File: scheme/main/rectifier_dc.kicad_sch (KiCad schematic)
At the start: 30 parts, among them K1 G2RL-1-E, Q2 BC847

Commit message: added L fuse & more
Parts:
- D15: footprint (none) -> LED_SMD:LED_0805_2012Metric
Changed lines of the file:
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@@
 			)
 		)
-		(property "Footprint" ""
+		(property "Footprint" "LED_SMD:LED_0805_2012Metric"
 			(at 250.19 74.93 0)
 			(effects

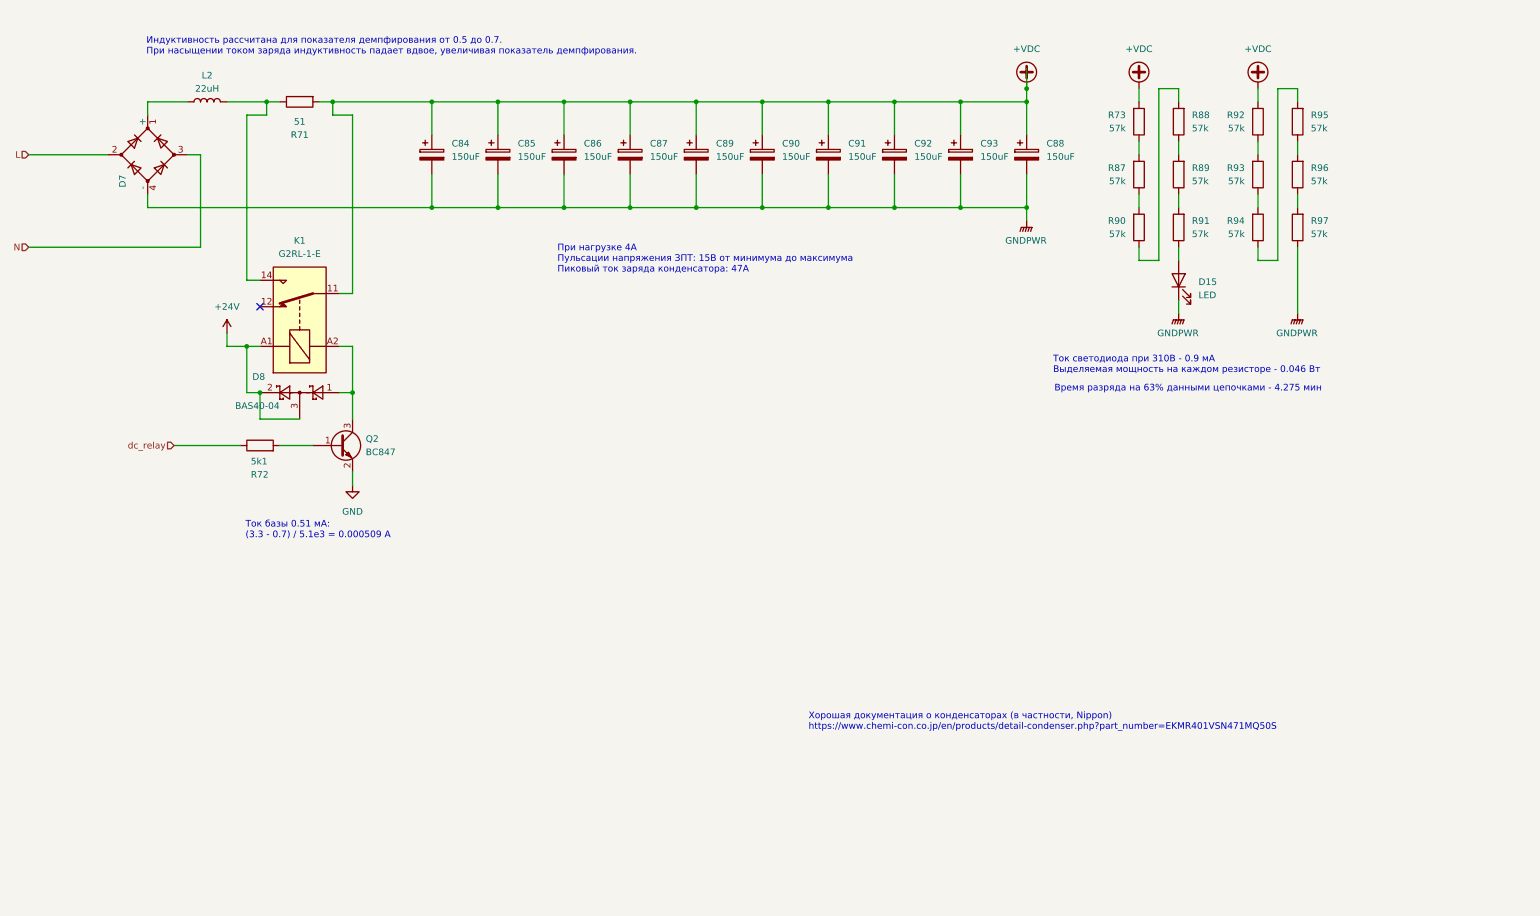
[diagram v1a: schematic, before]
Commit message: added 24V & GND to DO terminal & more
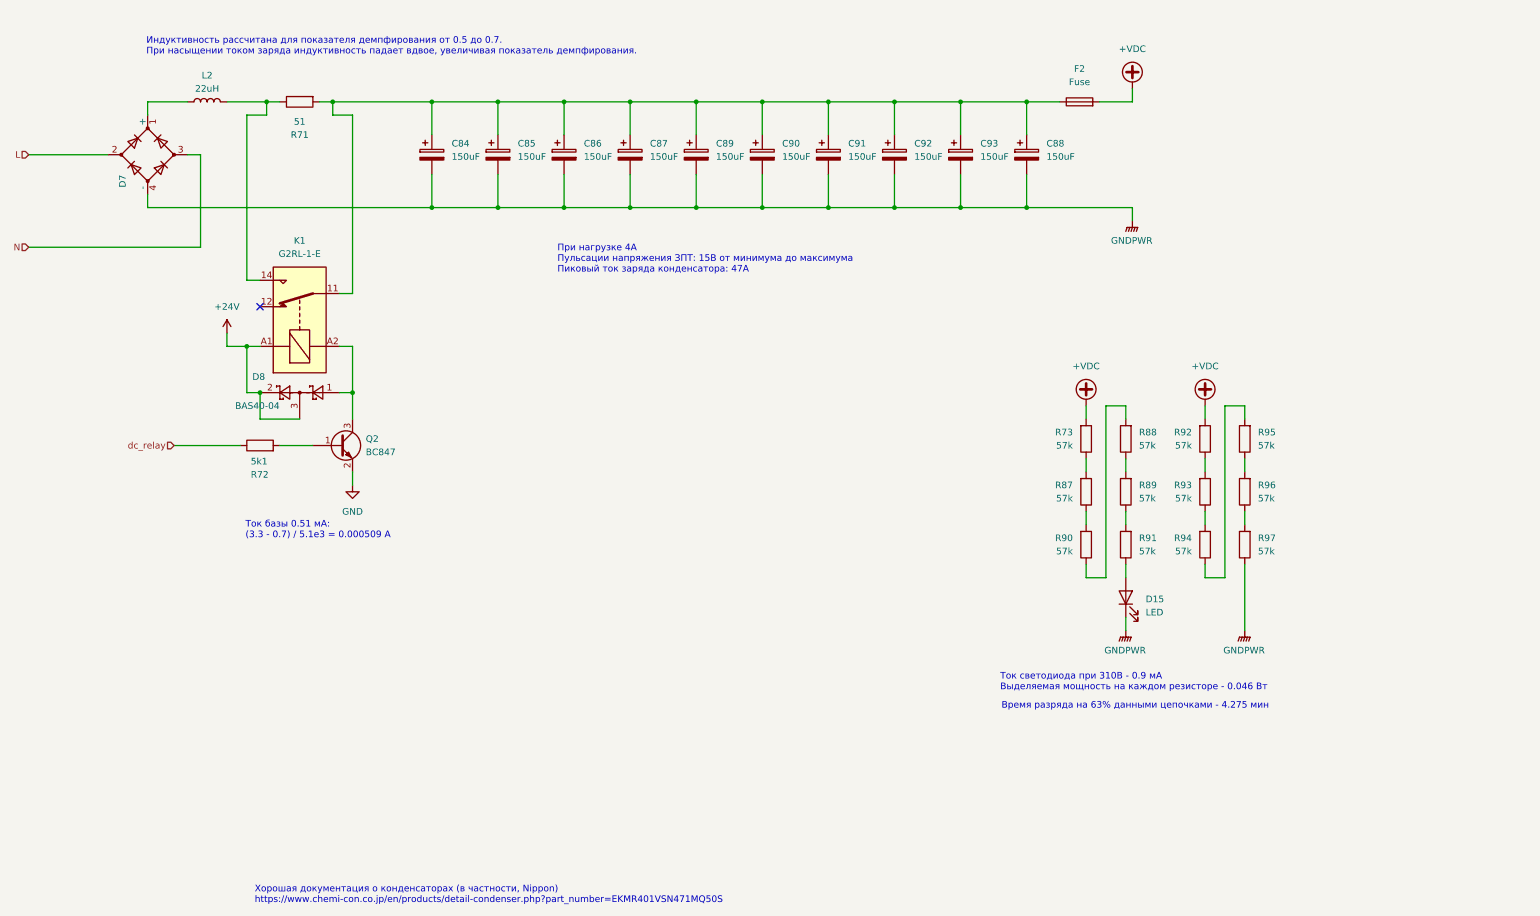
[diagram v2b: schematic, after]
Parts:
- added F2: Fuse, symbol Device:Fuse
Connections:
- net +VDC: now also F2.2; no longer C84.1, C85.1, C86.1, C87.1, C88.1, C89.1, C90.1, C91.1, C92.1, C93.1, K1.11, R71.2
- new net: C84.1, C85.1, C86.1, C87.1, C88.1, C89.1, C90.1, C91.1, C92.1, C93.1, F2.1, K1.11, R71.2
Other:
- moved on the sheet: D15, R73, R87, R88, R89, R90, R91, R92, R93, R94, R95, R96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

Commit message: sheets titles
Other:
- title: (none) -> Выпрямитель и звено постоянного тока
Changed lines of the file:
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@@
 	(generator_version "8.0")
 	(paper "A4")
+	(title_block
+		(title "Выпрямитель и звено постоянного тока")
+	)
 	(junction
 		(at 106.68 60.96)

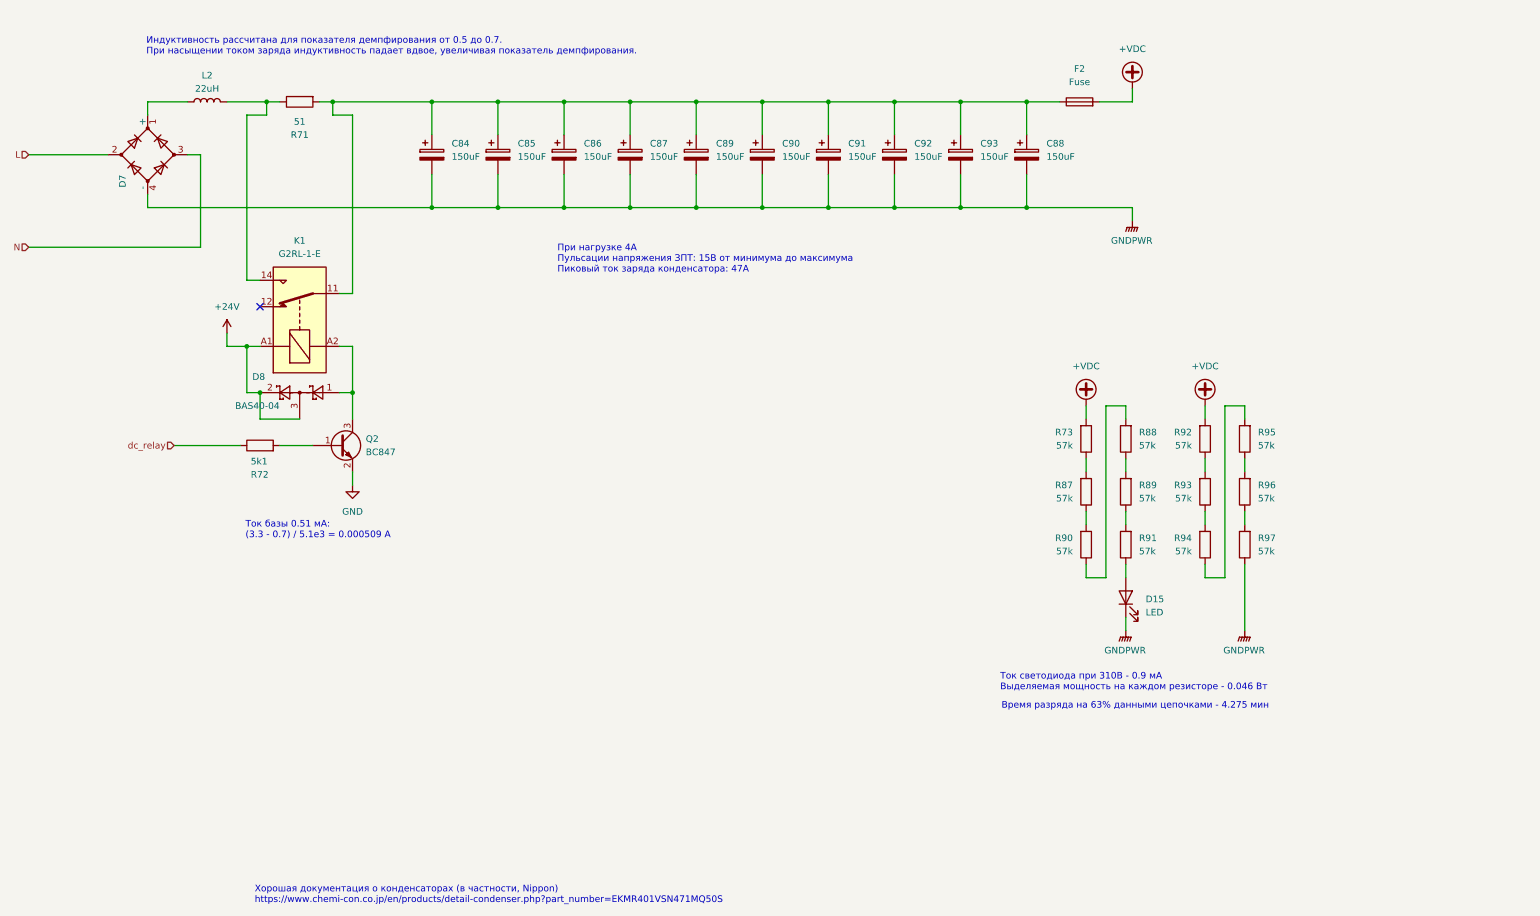
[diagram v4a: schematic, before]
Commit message: added fuses & inductanses
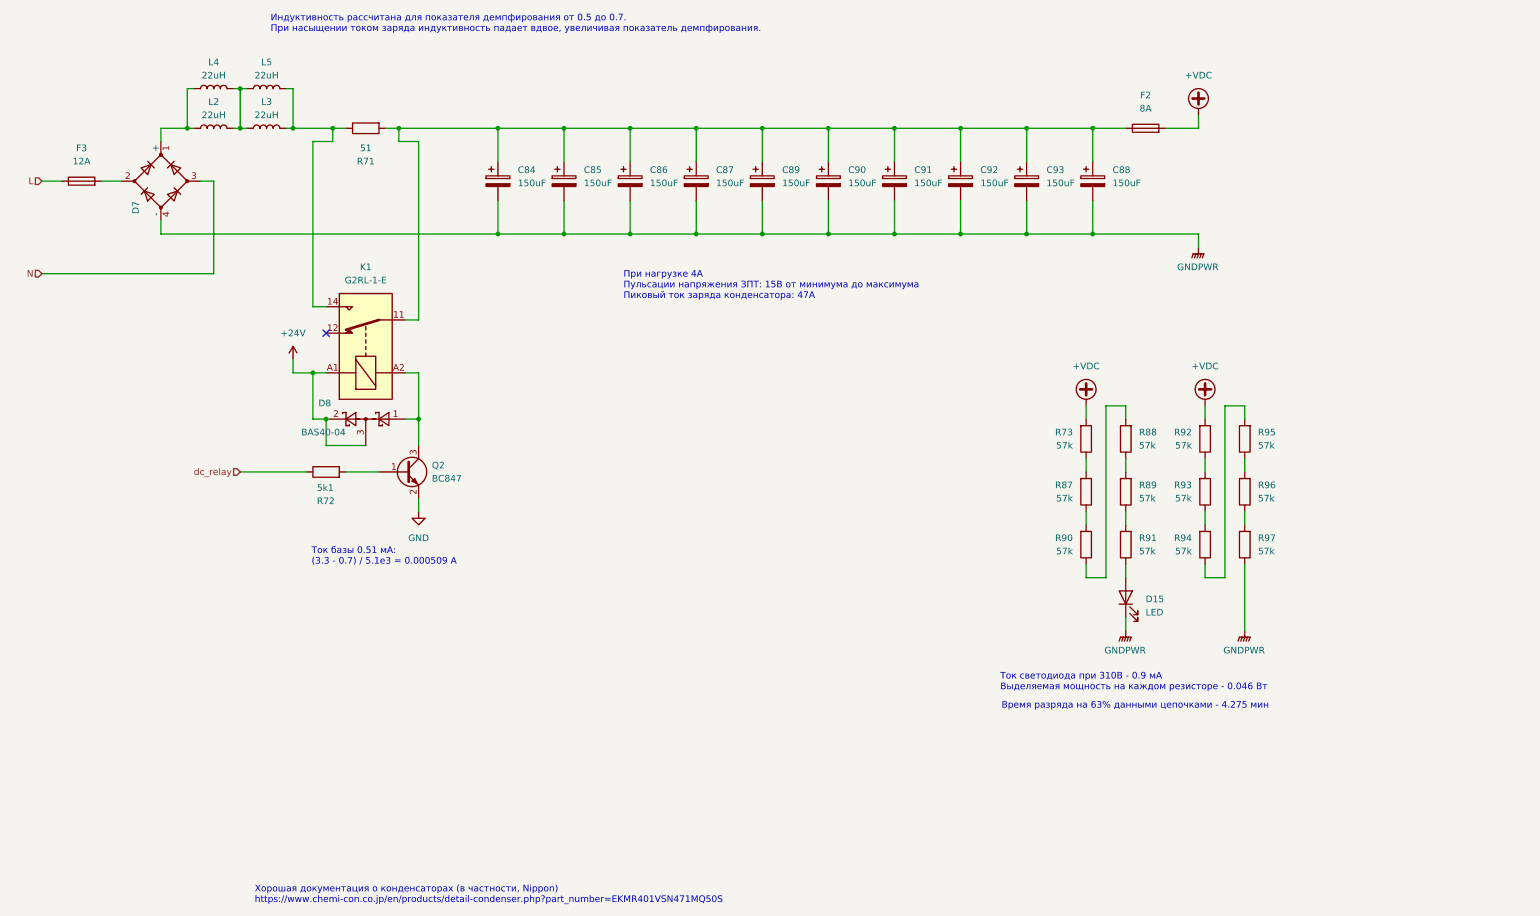
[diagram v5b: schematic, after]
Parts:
- added F3: 12A, symbol Device:Fuse
- added L3, L4, L5: 22uH, Inductor_SMD:L_Vishay_IHLP-6767, symbol Device:L
- F2: value Fuse -> 8A
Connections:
- net L: now also F3.1; no longer D7.2
- net at D7.1 (+), L2.1: now also L4.1
- net at K1.14, R71.1: now also L3.2, L5.2; no longer L2.2
- new net: D7.2, F3.2
- new net: L2.2, L3.1, L4.2, L5.1
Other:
- moved on the sheet: C84, C85, C86, C87, C88, C89, C90, C91, C92, C93, D7, D8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

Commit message: fixed check errors
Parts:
- removed F2: 8A, symbol Device:Fuse
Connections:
- net +VDC: now also C84.1, C85.1, C86.1, C87.1, C88.1, C89.1, C90.1, C91.1, C92.1, C93.1, K1.11, R71.2
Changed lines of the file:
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@@
 	)
 	(junction
+		(at 254 66.04)
+		(diameter 0)
+		(color 0 0 0 0)
+	)
+	(junction
 		(at 119.38 66.04)
 		(diameter 0)
@@
 	)
 	(junction
+		(at 254 45.72)
+		(diameter 0)
+		(color 0 0 0 0)
+	)
+	(junction
 		(at 182.88 45.72)
 		(diameter 0)
@@
 	(wire
 		(pts
+			(xy 262.89 45.72) (xy 254 45.72)
+		)
+		(stroke
+			(width 0)
+			(type default)
+		)
+	)
+	(wire
+		(pts
 			(xy 100.33 45.72) (xy 119.38 45.72)
 		)
@@
 	(wire
 		(pts
+			(xy 262.89 63.5) (xy 262.89 66.04)
+		)
+		(stroke
+			(width 0)
+			(type default)
+		)
+	)
+	(wire
+		(pts
+			(xy 262.89 66.04) (xy 254 66.04)
+		)
+		(stroke
+			(width 0)
+			(type default)
+		)
+	)
+	(wire
+		(pts
 			(xy 119.38 66.04) (xy 119.38 59.69)
 		)
@@
 	(wire
 		(pts
-			(xy 233.68 45.72) (xy 240.03 45.72)
+			(xy 233.68 45.72) (xy 254 45.72)
 		)
 		(stroke
@@
 	(wire
 		(pts
-			(xy 247.65 45.72) (xy 254 45.72)
-		)
-		(stroke
-			(width 0)
-			(type default)
-		)
-	)
-	(wire
-		(pts
 			(xy 43.18 55.88) (xy 46.99 55.88)
 		)
@@
 	(wire
 		(pts
+			(xy 262.89 43.18) (xy 262.89 45.72)
+		)
+		(stroke
+			(width 0)
+			(type default)
+		)
+	)
+	(wire
+		(pts
 			(xy 255.27 99.06) (xy 255.27 101.6)
 		)
@@
 	)
 	(symbol
+		(lib_id "power:PWR_FLAG")
+		(at 262.89 43.18 0)
+		(unit 1)
+		(exclude_from_sim no)
+		(in_bom yes)
+		(on_board yes)
+		(dnp no)
+		(fields_autoplaced yes)
+		(property "Reference" "#FLG06"
+			(at 262.89 41.275 0)
+			(effects
+				(font
+					(size 1.27 1.27)
+				)
+				(hide yes)
+			)
+		)
+		(property "Value" "PWR_FLAG"
+			(at 262.89 38.1 0)
+			(effects
+				(font
+					(size 1.27 1.27)
+				)
+			)
+		)
+		(property "Footprint" ""
+			(at 262.89 43.18 0)
+			(effects
+				(font
+					(size 1.27 1.27)
+				)
+				(hide yes)
+			)
+		)
+		(property "Datasheet" "~"
+			(at 262.89 43.18 0)
+			(effects
+				(font
+					(size 1.27 1.27)
+				)
+				(hide yes)
+			)
+		)
+		(property "Description" "Special symbol for telling ERC where power comes from"
+			(at 262.89 43.18 0)
+			(effects
+				(font
+					(size 1.27 1.27)
+				)
+				(hide yes)
+			)
+		)
+		(pin "1"
+		)
+		(instances
+			(project "main"
+				(path "/c11d1dbc-4db9-4712-8d1d-5f6f7086cded/529e7c08-d17e-4397-8cce-ee2a0c13f81d"
+					(reference "#FLG06")
+					(unit 1)
+				)
+			)
+		)
+	)
+	(symbol
 		(lib_id "power:GNDPWR")
 		(at 262.89 142.24 0)
@@
 	)
 	(symbol
-		(lib_id "Device:Fuse")
-		(at 243.84 45.72 90)
-		(unit 1)
-		(exclude_from_sim no)
-		(in_bom yes)
-		(on_board yes)
-		(dnp no)
-		(fields_autoplaced yes)
-		(property "Reference" "F2"
-			(at 243.84 39.37 90)
-			(effects
-				(font
-					(size 1.27 1.27)
-				)
-			)
-		)
-		(property "Value" "8A"
-			(at 243.84 41.91 90)
-			(effects
-				(font
-					(size 1.27 1.27)
-				)
-			)
-		)
-		(property "Footprint" ""
-			(at 243.84 47.498 90)
-			(effects
-				(font
-					(size 1.27 1.27)
-				)
-				(hide yes)
-			)
-		)
-		(property "Datasheet" "~"
-			(at 243.84 45.72 0)
-			(effects
-				(font
-					(size 1.27 1.27)
-				)
-				(hide yes)
-			)
-		)
-		(property "Description" "Fuse"
-			(at 243.84 45.72 0)
-			(effects
-				(font
-					(size 1.27 1.27)
-				)
-				(hide yes)
-			)
-		)
-		(pin "1"
-		)
-		(pin "2"
-		)
-		(instances
-			(project ""
-				(path "/c11d1dbc-4db9-4712-8d1d-5f6f7086cded/529e7c08-d17e-4397-8cce-ee2a0c13f81d"
-					(reference "F2")
-					(unit 1)
-				)
-			)
-		)
-	)
-	(symbol
 		(lib_id "power:+VDC")
 		(at 254 43.18 0)
@@
 					(unit 1)
 				)
+			)
+		)
+	)
+	(symbol
+		(lib_id "power:PWR_FLAG")
+		(at 262.89 63.5 0)
+		(unit 1)
+		(exclude_from_sim no)
+		(in_bom yes)
+		(on_board yes)
+		(dnp no)
+		(fields_autoplaced yes)
+		(property "Reference" "#FLG05"
+			(at 262.89 61.595 0)
+			(effects
+				(font
+					(size 1.27 1.27)
+				)
+				(hide yes)
+			)
+		)
+		(property "Value" "PWR_FLAG"
+			(at 262.89 58.42 0)
+			(effects
+				(font
+					(size 1.27 1.27)
+				)
+			)
+		)
+		(property "Footprint" ""
+			(at 262.89 63.5 0)
+			(effects
+				(font
+					(size 1.27 1.27)
+				)
+				(hide yes)
+			)
+		)
+		(property "Datasheet" "~"
+			(at 262.89 63.5 0)
+			(effects
+				(font
+					(size 1.27 1.27)
+				)
+				(hide yes)
+			)
+		)
+		(property "Description" "Special symbol for telling ERC where power comes from"
+			(at 262.89 63.5 0)
+			(effects
+				(font
+					(size 1.27 1.27)
+				)
+				(hide yes)
+			)
+		)
+		(pin "1"
+		)
+		(instances
+			(project "main"
+				(path "/c11d1dbc-4db9-4712-8d1d-5f6f7086cded/529e7c08-d17e-4397-8cce-ee2a0c13f81d"
+					(reference "#FLG05")
+					(unit 1)
+				)

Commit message: footprints set/changed
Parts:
- F3: footprint (none) -> main:Fuseholder_Clip-5x20mm_KLS5-266
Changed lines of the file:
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@@
 			)
 		)
-		(property "Footprint" ""
+		(property "Footprint" "main:Fuseholder_Clip-5x20mm_KLS5-266"
 			(at 39.37 57.658 90)
 			(effects
